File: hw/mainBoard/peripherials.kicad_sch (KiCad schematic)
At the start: 6 parts, among them U3 SC16IS752IPW, Y1 1.8432MHz

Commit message: hw - kicad neco
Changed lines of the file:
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@@
   )
   (symbol (lib_id "Interface_UART:SC16IS752IPW") (at 77.47 50.8 0) (unit 1)
-    (in_bom yes) (on_board yes) (dnp no) (fields_autoplaced)
+    (in_bom yes) (on_board yes) (dnp no)
     (property "Reference" "U3" (at 79.6641 22.86 0)
       (effects (font (size 1.27 1.27)) (justify left))
@@
       (effects (font (size 1.27 1.27)) hide)
     )
-    (property "Datasheet" "https://www.nxp.com/docs/en/data-sheet/SC16IS752_SC16IS762.pdf" (at 77.47 86.36 0)
-      (effects (font (size 1.27 1.27)) hide)
+    (property "Datasheet" "https://www.nxp.com/docs/en/data-sheet/SC16IS752_SC16IS762.pdf" (at 114.3 77.47 0)
+      (effects (font (size 1.27 1.27)))
     )
     (pin "4")

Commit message: hw
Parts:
- removed C10: 22uF, symbol Device:C
- removed C8: 33pF, symbol Device:C
- removed C9: 22pF, symbol Device:C
- removed U3: SC16IS752IPW, Package_SO:TSSOP-28_4.4x9.7mm_P0.65mm, symbol Interface_UART:SC16IS752IPW
- removed Y1: 1.8432MHz, symbol Device:Crystal
- added F1, F2, F3, F4: 1210L005WR, symbol Device:Polyfuse
- added F5: 30R400UMR, symbol Device:Polyfuse
- added J4: Per_Conn1, symbol Connector:Conn_01x06_Pin
- added J4: Per_Conn2, symbol Connector:Conn_01x06_Pin
- added R11, R12, R13: 330, symbol Device:R
- added U5: SRDA3.3-4DR2G, SOIC8_4X5_ONS, symbol SRDA3.3-4:SRDA3.3-4DR2G
- R3: value 1k -> 330
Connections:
- net 3V3: now also U5.2 (REF1), U5.3 (REF1); no longer R3.1
- net GND: now also J4.2 (Pin_2), J4.2 (Pin_2), J4.4 (Pin_4), J4.4 (Pin_4), U5.5 (GND), U5.8 (GND)
- net ~{UART_INT} renamed RX2
- net RX2: now also F4.1, U5.7 (I/O4)
- new net: F4.2, J4.6 (Pin_6)
- new net: F1.2, J4.5 (Pin_5)
- new net: F2.2, J4.6 (Pin_6)
- new net: F3.2, J4.5 (Pin_5)
- new net 24V_FUSED: F5.2, J4.1 (Pin_1), J4.1 (Pin_1)
- new net 5.2V: J4.3 (Pin_3), J4.3 (Pin_3)
- new net EXT_24V: F5.1
- new net RX1: F2.1, R12.2, U5.4 (I/O2)
- new net TX1: F1.1, R13.2, U5.1 (I/O1)
- new net TX2: F3.1, R11.2, U5.6 (I/O3)
- new net UART1_RX: R12.1
- new net UART1_TX: R13.1
- new net UART2_RX: R3.1
- new net UART2_TX: R11.1
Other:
- note added: "Hold 4A Trip 8A"
- note added: "Hold 50mA Trip 150mA"
- note added: "Protecting diodes IC"
- note removed: "Value choosed by myself"

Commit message: hw + blok schema
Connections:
- net 24V_FUSED: no longer names the net of F5.2, J4.1 (Pin_1), J4.1 (Pin_1)
- net EXT_24V renamed 24V
- net RX1: no longer names the net of F2.1, R12.2, U5.4 (I/O2)
- net RX2: no longer names the net of F4.1, R3.2, U5.7 (I/O4)
- net TX1: no longer names the net of F1.1, R13.2, U5.1 (I/O1)
- net TX2: no longer names the net of F3.1, R11.2, U5.6 (I/O3)
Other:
- moved on the sheet: F1, F2, F3, F4, F5, J4, R11, R12, R13, R3, U5

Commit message: nejaky hw + teorie + desky
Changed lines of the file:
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@@
     (effects (font (size 1.27 1.27)) (justify right bottom))
   )
-  (hierarchical_label "UART2" (shape bidirectional) (at 83.82 86.36 180) (fields_autoplaced)
+  (hierarchical_label "{UART2}" (shape bidirectional) (at 83.82 86.36 180) (fields_autoplaced)
     (effects (font (size 1.27 1.27)) (justify right))
   )
-  (hierarchical_label "UART1" (shape bidirectional) (at 83.82 55.88 180) (fields_autoplaced)
+  (hierarchical_label "{UART1}" (shape bidirectional) (at 83.82 55.88 180) (fields_autoplaced)
     (effects (font (size 1.27 1.27)) (justify right))
   )

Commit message: hw - rezistory
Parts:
- added F6: SMD1812B110TF/24, symbol Device:Polyfuse
- F1, F2, F3, F4: value 1210L005WR -> 0ZCM0002FF2G
- R11, R12, R13, R3: value 330 -> 100R
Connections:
- net 5.2V: now also F6.1; no longer J4.3 (Pin_3), J4.3 (Pin_3)
- new net: F6.2, J4.3 (Pin_3), J4.3 (Pin_3)
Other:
- note added: "Hold 1.1A Trip 1.95A"
- note added: "Hold 20mA Trip 60mA"
- note removed: "Hold 50mA Trip 150mA"
- moved on the sheet: U5

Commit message: drawing layout
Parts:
- removed F1, F2, F3, F4: 0ZCM0002FF2G, symbol Device:Polyfuse
- removed J4: Per_Conn1, symbol Connector:Conn_01x06_Pin
- removed J4: Per_Conn2, symbol Connector:Conn_01x06_Pin
- removed R11, R12, R13, R3: 100R, symbol Device:R
- removed U5: SRDA3.3-4DR2G, SOIC8_4X5_ONS, symbol SRDA3.3-4:SRDA3.3-4DR2G
- added C11, C12: 0.1uF, Capacitor_SMD:C_1206_3216Metric_Pad1.33x1.80mm_HandSolder, symbol Device:C
- added IC1: ATA6561-GAQW-N, ATA6561-GAQW-N:SOIC127P600X175-8N, symbol ATA6561-GAQW-N:ATA6561-GAQW-N
- added J2, J4: G17C0900132EU, G17C0900132EU, symbol DSUB-G17C9001:G17C0900132EU
- F5: footprint (none) -> 30R400UMR:30R400UMR
- F6: footprint (none) -> Fuse:Fuse_1812_4532Metric
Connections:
- net 3V3: now also C12.1, IC1.5 (VIO)
- net 5.2V: now also C11.1, IC1.3 (VCC)
- net GND: now also C11.2, C12.2, IC1.2 (GND), J2.1, J2.5, J2.6, J2.9, J4.1, J4.5, J4.6, J4.9
- net at F5.2: now also J2.2, J2.7, J4.2, J4.7
- net at F6.2: now also J2.8, J4.8
- new net: IC1.7 (CANH), J2.3, J4.3
- new net: IC1.6 (CANL), J2.4, J4.4
- new net CAN_RX: IC1.4 (RXD)
- new net CAN_STBY: IC1.8 (STBY)
- new net CAN_TX: IC1.1 (TXD)
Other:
- note added: "1 GND_P 6 GND_P 2 24V 7 24V 3 CANH 8 5.2V 4 CANL 9 GND_DATA 5 GND_DATA"
- note removed: "Hold 20mA Trip 60mA"
- note removed: "Protecting diodes IC"
- moved on the sheet: F5, F6

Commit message: finale bez rybicky
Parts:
- J1: renamed from J2; footprint G17C0900132EU -> DSUB-G17C09001:G17C0900132EU
- J2: renamed from J4; footprint G17C0900132EU -> DSUB-G17C09001:G17C0900132EU
- renumbered C12 to C6, C11 to C7, F6 to F1, F5 to F2
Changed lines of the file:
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@@
   (symbol (lib_id "DSUB-G17C9001:G17C0900132EU") (at 187.96 127 90) (unit 1)
     (in_bom yes) (on_board yes) (dnp no)
-    (property "Reference" "J4" (at 187.96 101.6 90)
+    (property "Reference" "J2" (at 187.96 101.6 90)
       (effects (font (size 1.27 1.27)) (justify right))
     )
@@
       (effects (font (size 1.27 1.27)) (justify right))
     )
-    (property "Footprint" "G17C0900132EU" (at 277.8 105.41 0)
+    (property "Footprint" "DSUB-G17C09001:G17C0900132EU" (at 277.8 105.41 0)
       (effects (font (size 1.27 1.27)) (justify left top) hide)
     )
@@
       (project "mainBoard"
         (path "/afbe4b5f-4e5c-4a12-a44b-208d158a3f7a/9f509f3e-56fd-407b-8646-52f67dc756e2"
-          (reference "J4") (unit 1)
+          (reference "J2") (unit 1)
         )
       )
@@
   (symbol (lib_id "Device:Polyfuse") (at 105.41 43.18 90) (unit 1)
     (in_bom yes) (on_board yes) (dnp no) (fields_autoplaced)
-    (property "Reference" "F5" (at 105.41 36.83 90)
+    (property "Reference" "F2" (at 105.41 36.83 90)
       (effects (font (size 1.27 1.27)))
     )
@@
       (project "mainBoard"
         (path "/afbe4b5f-4e5c-4a12-a44b-208d158a3f7a/9f509f3e-56fd-407b-8646-52f67dc756e2"
-          (reference "F5") (unit 1)
+          (reference "F2") (unit 1)
         )
       )
@@
   (symbol (lib_id "Device:C") (at 127 88.9 0) (unit 1)
     (in_bom yes) (on_board yes) (dnp no)
-    (property "Reference" "C12" (at 129.54 88.9 0)
+    (property "Reference" "C6" (at 129.54 88.9 0)
       (effects (font (size 1.27 1.27)) (justify left))
     )
@@
       (project "mainBoard"
         (path "/afbe4b5f-4e5c-4a12-a44b-208d158a3f7a/9f509f3e-56fd-407b-8646-52f67dc756e2"
-          (reference "C12") (unit 1)
+          (reference "C6") (unit 1)
         )
       )
@@
   (symbol (lib_id "DSUB-G17C9001:G17C0900132EU") (at 187.96 91.44 90) (unit 1)
     (in_bom yes) (on_board yes) (dnp no)
-    (property "Reference" "J2" (at 187.96 66.04 90)
+    (property "Reference" "J1" (at 187.96 66.04 90)
       (effects (font (size 1.27 1.27)) (justify right))
     )
@@
       (effects (font (size 1.27 1.27)) (justify right))
     )
-    (property "Footprint" "G17C0900132EU" (at 277.8 69.85 0)
+    (property "Footprint" "DSUB-G17C09001:G17C0900132EU" (at 277.8 69.85 0)
       (effects (font (size 1.27 1.27)) (justify left top) hide)
     )
@@
       (project "mainBoard"
         (path "/afbe4b5f-4e5c-4a12-a44b-208d158a3f7a/9f509f3e-56fd-407b-8646-52f67dc756e2"
-          (reference "J2") (unit 1)
+          (reference "J1") (unit 1)
         )
       )
@@
   (symbol (lib_id "Device:C") (at 96.52 88.9 0) (unit 1)
     (in_bom yes) (on_board yes) (dnp no)
-    (property "Reference" "C11" (at 99.06 88.9 0)
+    (property "Reference" "C7" (at 99.06 88.9 0)
       (effects (font (size 1.27 1.27)) (justify left))
     )
@@
       (project "mainBoard"
         (path "/afbe4b5f-4e5c-4a12-a44b-208d158a3f7a/9f509f3e-56fd-407b-8646-52f67dc756e2"
-          (reference "C11") (unit 1)
+          (reference "C7") (unit 1)
         )
       )
@@
   (symbol (lib_id "Device:Polyfuse") (at 105.41 55.88 90) (unit 1)
     (in_bom yes) (on_board yes) (dnp no) (fields_autoplaced)
-    (property "Reference" "F6" (at 105.41 49.53 90)
+    (property "Reference" "F1" (at 105.41 49.53 90)
       (effects (font (size 1.27 1.27)))
     )
@@
       (project "mainBoard"
         (path "/afbe4b5f-4e5c-4a12-a44b-208d158a3f7a/9f509f3e-56fd-407b-8646-52f67dc756e2"
-          (reference "F6") (unit 1)
-        )
-      )
+          (reference "F1") (unit 1)
+        )
+      )

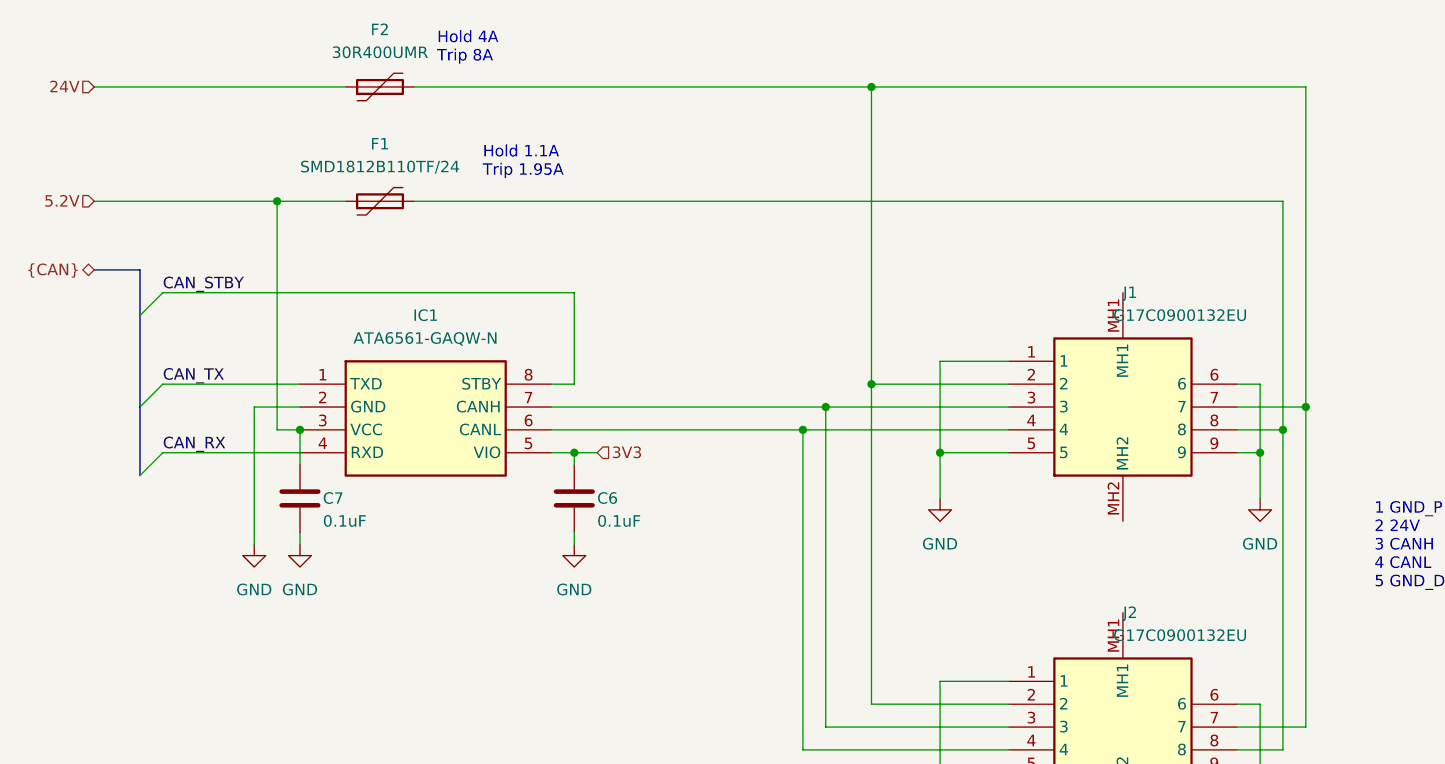
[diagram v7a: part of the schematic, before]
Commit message: text - periferie, obrazky hw - schemata
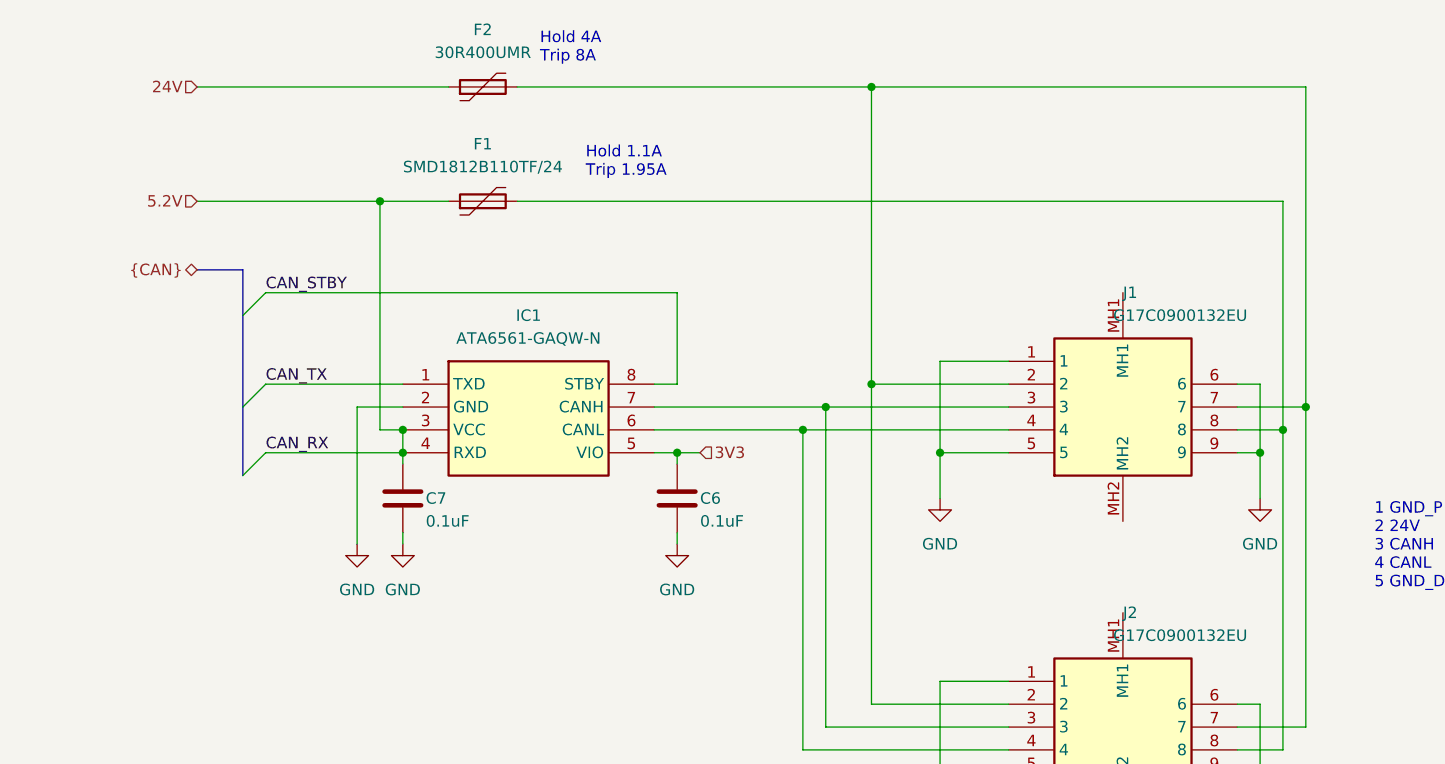
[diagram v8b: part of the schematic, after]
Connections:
- net CAN_RX is gone; now on net 5.2V: IC1.4 (RXD)
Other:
- moved on the sheet: C6, C7, F1, F2, IC1
